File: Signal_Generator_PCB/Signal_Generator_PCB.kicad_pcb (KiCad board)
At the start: 2 copper layers, 100 x 100 mm, 11 parts, among them J1 Conn_01x04, J2 Conn_01x02, SW1 RotaryEncoder_Switch, U1 ESP32-DevKitC

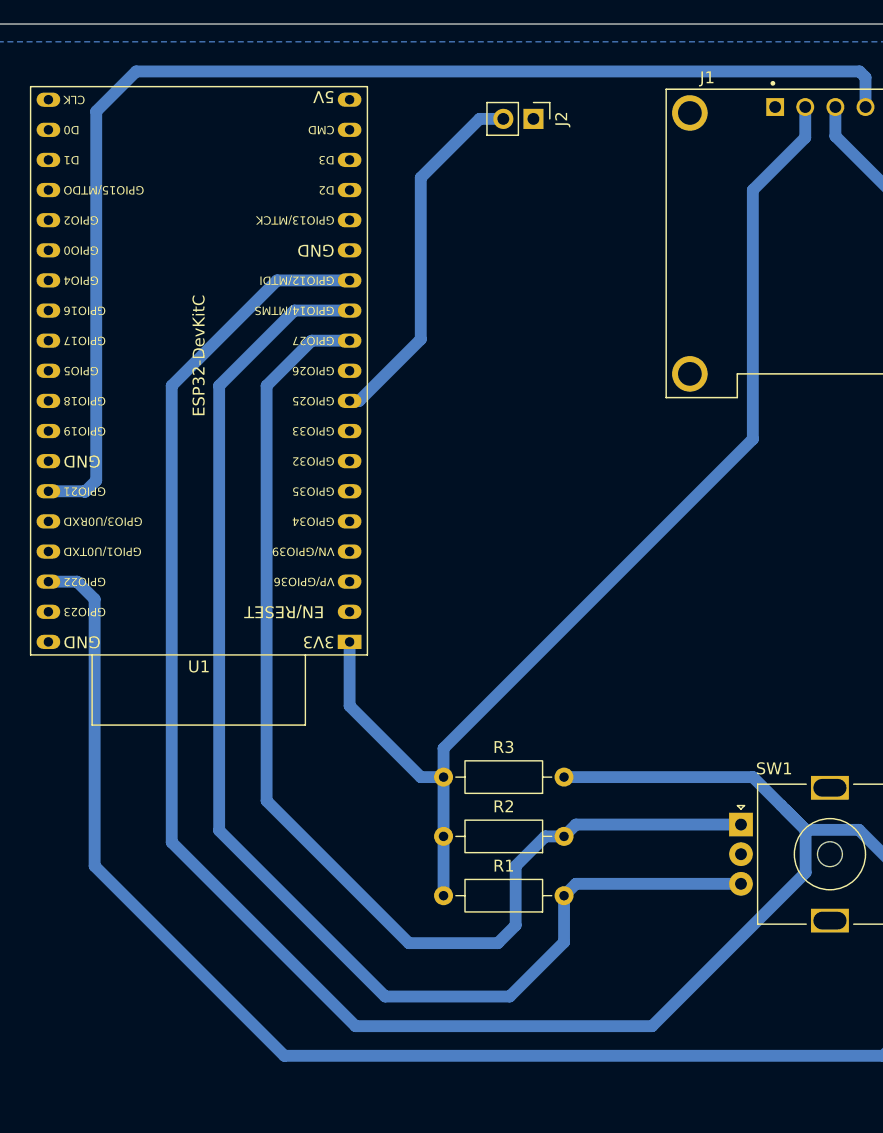
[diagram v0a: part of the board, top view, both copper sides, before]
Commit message: feat(Signal_Generator): Añado los header files.
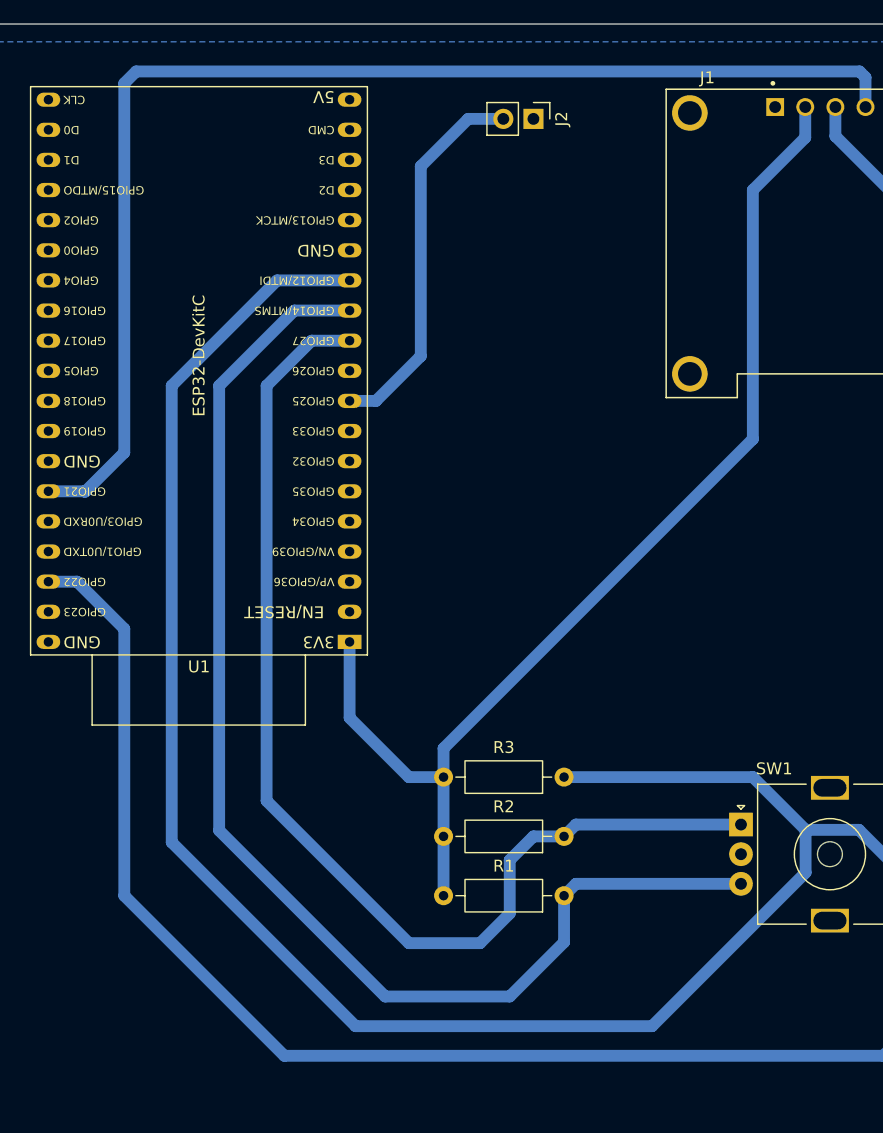
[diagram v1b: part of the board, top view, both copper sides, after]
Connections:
- REF** pad 1: GNDREF -> (no net) (x4)
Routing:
- net /GPIO12: track 161.6 -> 159.2 mm
- net /GPIO25: track 30.8 -> 32.2 mm
- net +3.3V: track 94.9 -> 95.5 mm

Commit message: feat(Signal_Generator_PCB): v02
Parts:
- removed the REF** at (150.0, 135.5)
- removed the REF** at (150.0, 44.5)
- removed the REF** at (59.0, 135.5)
- removed the REF** at (59.0, 44.5)
- added G***: LOGO, LOGO, B.Cu at (152.5, 94.0)
- added G***: LOGO, LOGO, B.Cu at (114.0, 140.0)
- added REF**: MountingHole_2.2mm_M2_DIN965_Pad_TopBottom, MountingHole:MountingHole_2.2mm_M2_DIN965_Pad_TopBottom, F.Cu at (105.0, 149.5)
- added REF**: MountingHole_2.2mm_M2_DIN965_Pad_TopBottom, MountingHole:MountingHole_2.2mm_M2_DIN965_Pad_TopBottom, F.Cu at (105.0, 58.5)
- added REF**: MountingHole_2.2mm_M2_DIN965_Pad_TopBottom, MountingHole:MountingHole_2.2mm_M2_DIN965_Pad_TopBottom, F.Cu at (196.0, 149.5)
- added REF**: MountingHole_2.2mm_M2_DIN965_Pad_TopBottom, MountingHole:MountingHole_2.2mm_M2_DIN965_Pad_TopBottom, F.Cu at (196.0, 58.5)
- moved R1 48.1 mm to (155.6, 127.5)
- moved R2 48.1 mm to (155.6, 122.5)
- moved R3 48.1 mm to (155.6, 117.5)
- moved J1 48.1 mm to (177.2, 72.5)
- moved J2 48.1 mm to (153.0, 62.0)
- moved SW1 48.1 mm to (170.5, 121.5)
- moved U1 48.1 mm to (137.5, 106.1)
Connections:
- J1 pad 1: GNDREF -> GND
- J1 pad S1: GNDREF -> (no net)
- J1 pad S2: GNDREF -> (no net)
- J1 pad S3: GNDREF -> (no net)
- J1 pad S4: GNDREF -> (no net)
- J2 pad 1: GNDREF -> /GPIO25
- J2 pad 2: /GPIO25 -> GND
- SW1 pad C: GNDREF -> GND
- SW1 pad S2: GNDREF -> GND
- U1 pad 14: GNDREF -> GND
- U1 pad 19: unconnected-(U1-5V-Pad19) -> +5V
- U1 pad 32: GNDREF -> GND
- U1 pad 38: GNDREF -> GND
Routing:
- net +3.3V: track 95.5 -> 104.4 mm
- added copper zone on B.Cu, net GND
- removed copper zone on B.Cu, net GNDREF
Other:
- board text added: "GND"
- board text added: "OUT"

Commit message: feat(Signal_Generator): Primer Versión Parcial del Código
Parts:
- moved G*** 4.24 mm to (155.5, 91.0)
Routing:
- net +3.3V: track 104.4 -> 105.8 mm
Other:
- board text added: "Fausto Alvarez Mollo"

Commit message: feat(PCB): Cambios en la configuración de la PCB.
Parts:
- removed the G*** at (155.5, 91.0)
- added G***: LOGO, images:utn_logo, B.Cu at (155.2, 91.0)
- J1: value Conn_01x04 -> OLED Screen
- SW1: value RotaryEncoder_Switch -> Rotary Encoder with Switch
- moved U1 3.01 mm to (137.4, 109.1)
- moved SW1 0.40 mm to (170.5, 121.9)
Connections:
- R3 pad 1: /GPIO12 -> /GPIO32
- SW1 pad S1: /GPIO12 -> /GPIO32
- U1 pad 13: /GPIO12 -> unconnected-(U1-MTDI/GPIO12/ADC2_CH5-Pad13)
- U1 pad 7: unconnected-(U1-32K_XP/GPIO32/ADC1_CH4-Pad7) -> /GPIO32
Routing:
- net /GPIO12: track 159.2 -> 0.00 mm
- net /GPIO32: track 0.00 -> 106.6 mm
- net /GPIO27: track 95.3 -> 103.3 mm
- net /GPIO14: track 107.2 -> 111.2 mm
- net /GPIO21: track 104.5 -> 108.1 mm
- net /GPIO25: track 32.2 -> 35.6 mm
- net +3.3V: track 105.8 -> 102.5 mm
- net /GPIO22: track 188.9 -> 187.0 mm

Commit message: feat(PCB): Redistribuyo y embellezco la placa
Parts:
- removed the G*** at (114.0, 140.0)
- added kobee-studio-6AAF543E: Kobee Studio, kobee-studio-6AAF5432, B.Cu at (151.5, 103.1)
- added kobee-studio-6AAF54B1: Kobee Studio, kobee-studio-6AAF52F9, B.Cu at (111.8, 136.6)
- added kobee-studio-6AAF59F9: Kobee Studio, kobee-studio-6AAF59EB, B.Cu at (148.5, 70.5)
- added kobee-studio-6AAF5AC9: Kobee Studio, kobee-studio-6AAF5ABC, B.Cu at (151.0, 70.4)
- moved J1 4.31 mm to (175.2, 76.3)
- moved G*** 3.85 mm to (151.5, 92.0)
- moved J2 3.36 mm to (151.0, 64.7)
- moved R1 2.24 mm to (153.6, 128.5)
- moved R2 2.24 mm to (153.6, 123.5)
- moved R3 2.24 mm to (153.6, 118.5)
- moved REF** 2.24 mm to (103.0, 150.5)
- moved REF** 2.24 mm to (103.0, 59.5)
- moved REF** 2.24 mm to (194.0, 150.5)
- moved REF** 2.24 mm to (194.0, 59.5)
- moved SW1 2.24 mm to (168.5, 122.9)
- moved U1 2.24 mm to (135.4, 110.1)
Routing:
- net /GPIO22: track 187.0 -> 181.3 mm
- net +3.3V: track 102.5 -> 100.5 mm
- net /GPIO21: track 108.1 -> 106.3 mm
- net /GPIO32: track 106.6 -> 105.8 mm
- net /GPIO25: track 35.6 -> 34.9 mm
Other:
- board text removed: "Fausto Alvarez Mollo"
- board text removed: "GND"
- board text removed: "OUT"

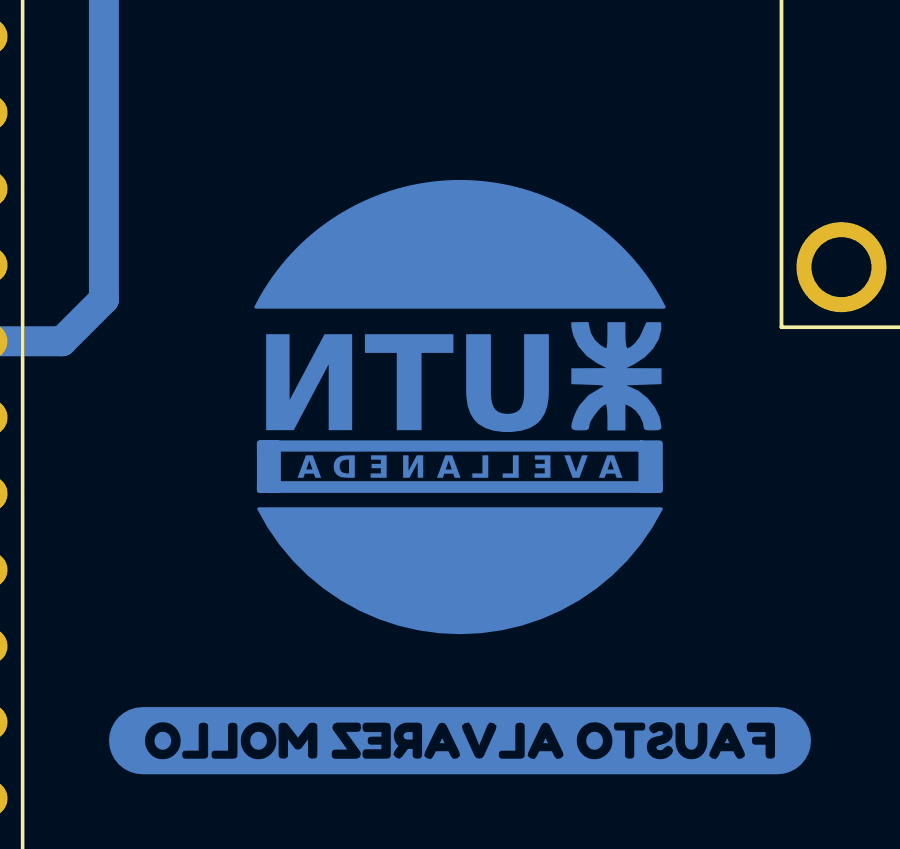
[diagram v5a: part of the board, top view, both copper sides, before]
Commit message: style(PCB): Cambio el Logo de la Universidad
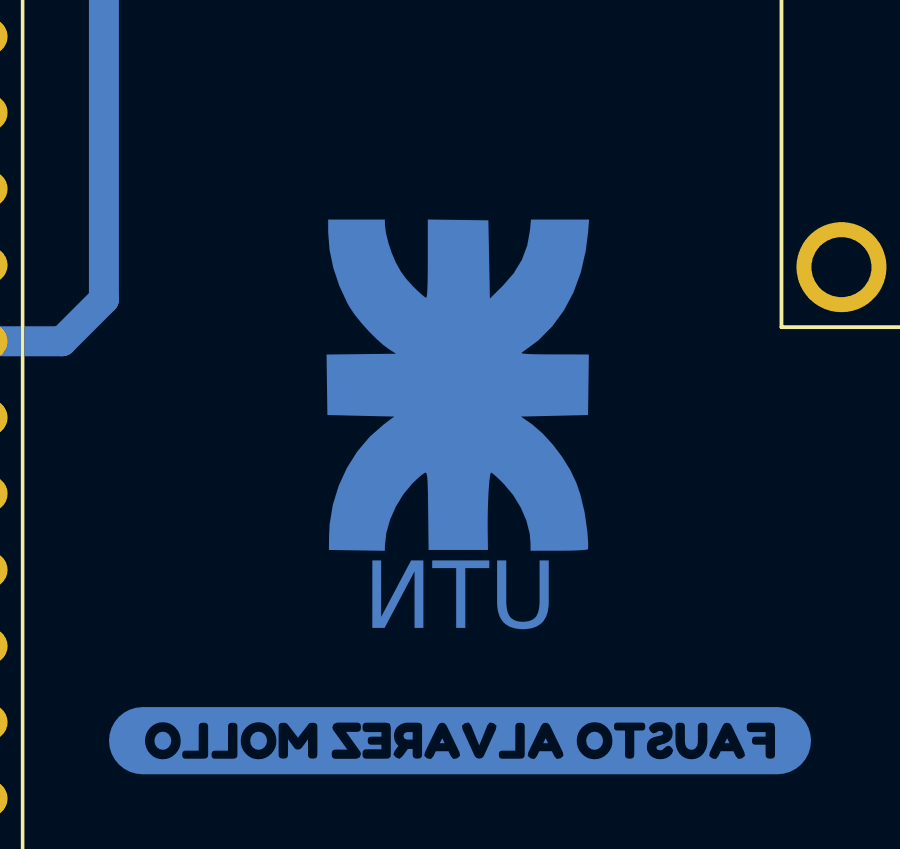
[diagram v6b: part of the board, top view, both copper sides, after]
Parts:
- removed the G*** at (151.5, 92.0)
- added G***: LOGO, LOGO, B.Cu at (151.5, 92.0)
